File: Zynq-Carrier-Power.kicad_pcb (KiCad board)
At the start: 2 copper layers, 49 x 41 mm, 36 parts, among them J1 Zynq_SoM, J10 Barrel_Jack_MountingPin, J2 B2B-PH-K-S, J3 USB_C_Receptacle_USB2.0_16P, J4 Conn_01x03, J5 Conn_01x03, J6 Conn_01x03, J7 Conn_01x02, J8 Conn_01x02, J9 Conn_01x03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

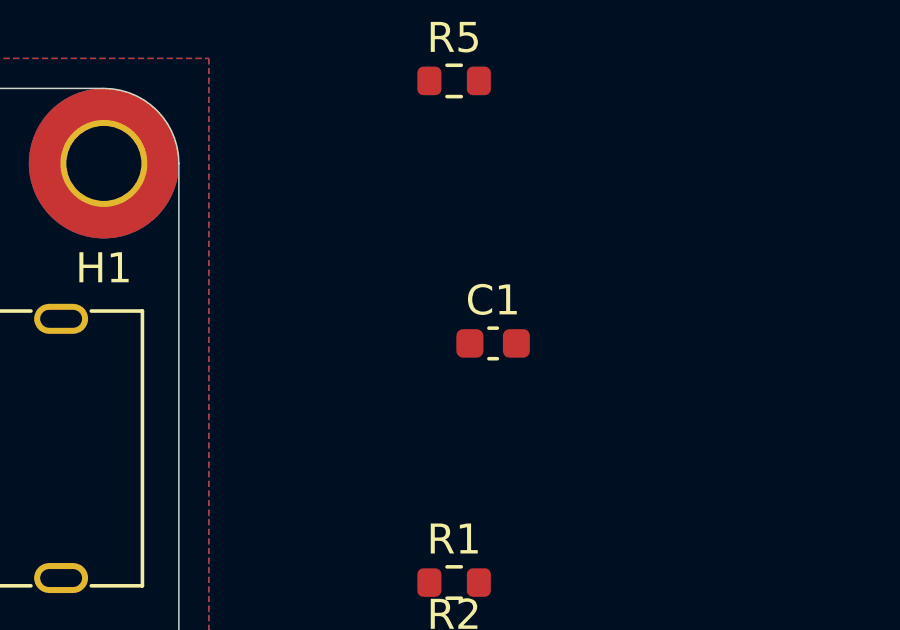
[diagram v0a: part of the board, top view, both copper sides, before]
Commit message: moved cap
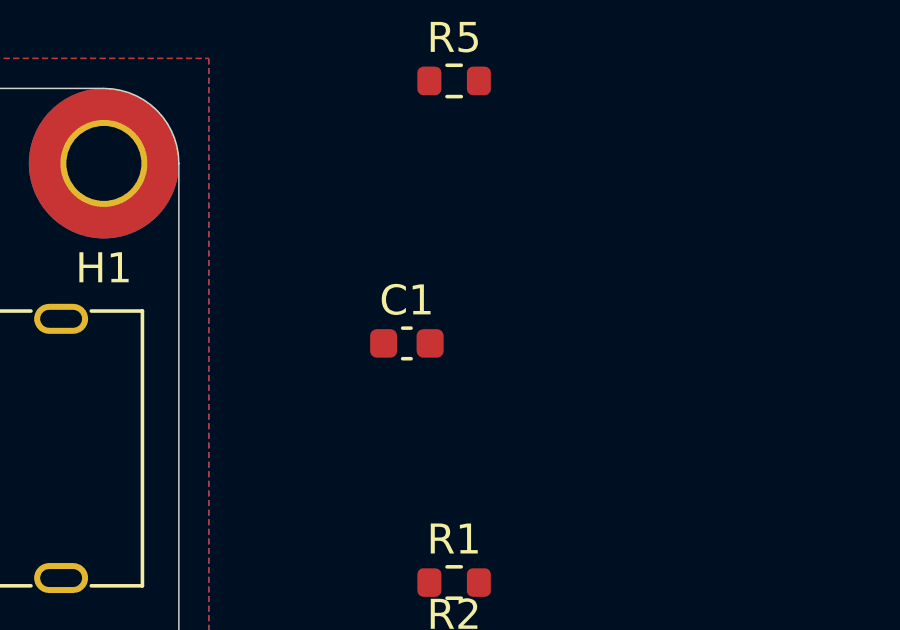
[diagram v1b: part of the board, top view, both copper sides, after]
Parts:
- moved C1 2.88 mm to (153.8, 109.1)
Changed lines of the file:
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@@
 	(footprint "Capacitor_SMD:C_0603_1608Metric"
 		(layer "F.Cu")
-		(at 156.700004 109.145)
+		(at 153.825004 109.145)
 		(descr "Capacitor SMD 0603 (1608 Metric), square (rectangular) end terminal, IPC-7351 nominal, (Body size source: IPC-SM-782 page 76, https://www.pcb-3d.com/wordpress/wp-content/uploads/ipc-sm-782a_amendment_1_and_2.pdf), generated with kicad-footprint-generator")
 		(tags "capacitor")

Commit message: Unmoved cap
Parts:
- moved C1 0.72 mm to (154.6, 109.1)
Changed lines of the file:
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@@
 	(footprint "Capacitor_SMD:C_0603_1608Metric"
 		(layer "F.Cu")
-		(at 153.825004 109.145)
+		(at 154.550004 109.145)
 		(descr "Capacitor SMD 0603 (1608 Metric), square (rectangular) end terminal, IPC-7351 nominal, (Body size source: IPC-SM-782 page 76, https://www.pcb-3d.com/wordpress/wp-content/uploads/ipc-sm-782a_amendment_1_and_2.pdf), generated with kicad-footprint-generator")
 		(tags "capacitor")
